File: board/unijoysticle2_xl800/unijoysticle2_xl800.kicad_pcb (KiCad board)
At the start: 4 copper layers, 72 x 53 mm, 54 parts, among them J1 USB_B_Micro, J2 DE9_Receptacle, J3 DE9_Receptacle, Q1 S8050, Q2 S8050, SW1 RESET, SW2 BOOT, SW3 MODE, SW4 SWAP, U1 ESP32-WROOM-32, U2 AMS1117-3.3, U3 CH340C, U4 74HC05, U5 74HC05, U6 74HC05

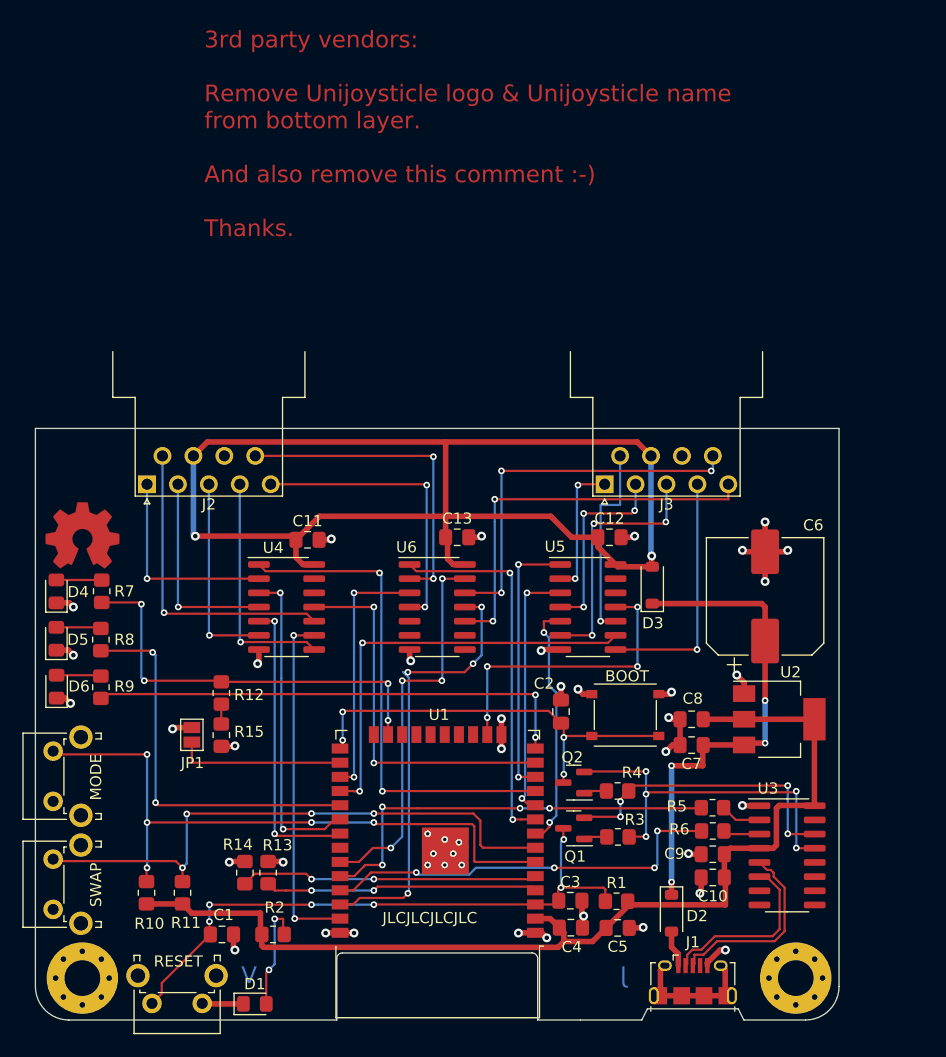
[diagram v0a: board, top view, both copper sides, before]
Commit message: 800XL Rev B.
Support Joy2Bplus buttons: similar to C64 Pot buttons.
GPIO36 Pull-up (instead of Pull-down) so that A500 can be differenciated
from 800XL.
Rounded corners at the top: might be needed if the DE9 connectors is
cut.
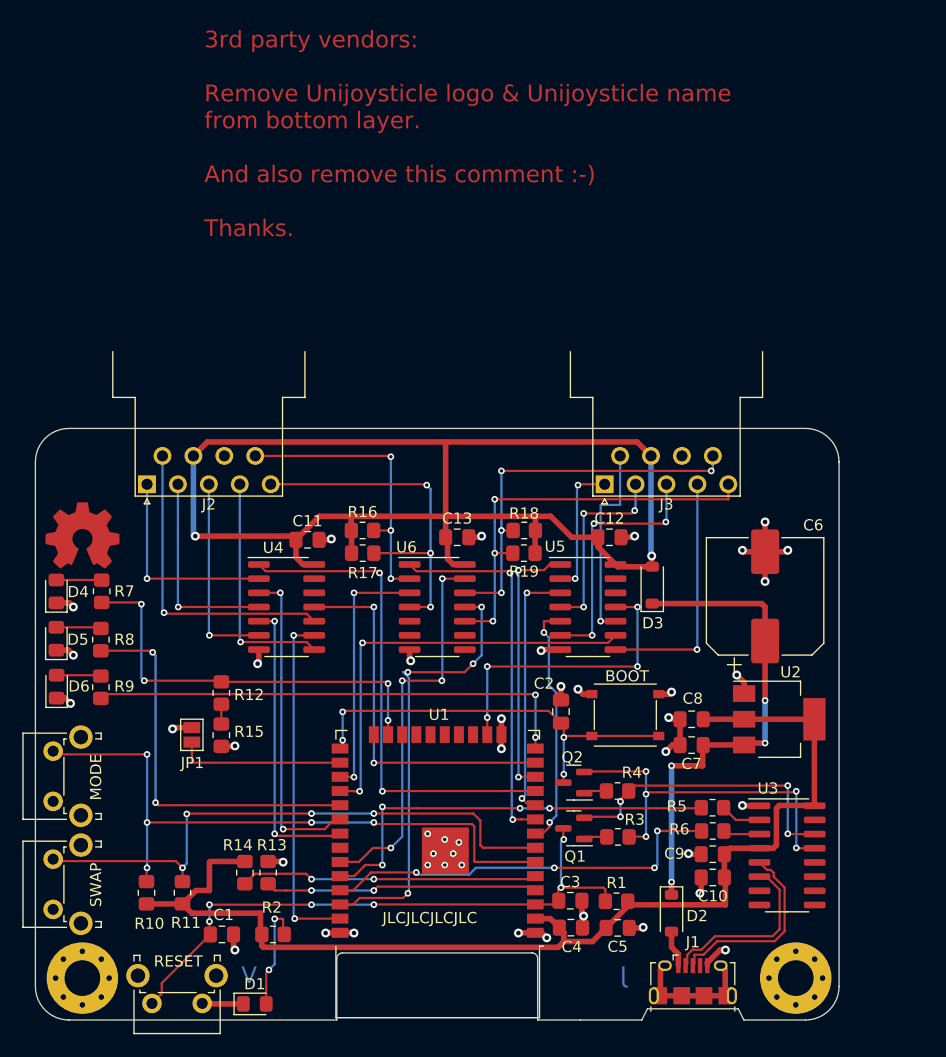
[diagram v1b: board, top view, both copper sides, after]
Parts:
- added R16: 2K7, Resistor_SMD:R_0805_2012Metric_Pad1.20x1.40mm_HandSolder, F.Cu at (106.8, 104.1)
- added R17: 2K7, Resistor_SMD:R_0805_2012Metric_Pad1.20x1.40mm_HandSolder, F.Cu at (106.8, 106.2)
- added R18: 2K7, Resistor_SMD:R_0805_2012Metric_Pad1.20x1.40mm_HandSolder, F.Cu at (121.3, 104.1)
- added R19: 2K7, Resistor_SMD:R_0805_2012Metric_Pad1.20x1.40mm_HandSolder, F.Cu at (121.3, 106.2)
- R14: value 0 -> 10K
- turned R14 to 90 degrees
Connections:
- R14 pad 1: GND -> GPIO_39
- R14 pad 2: GPIO_39 -> +3V3
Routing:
- net +3V3: track 95.2 -> 103.8 mm
- net +5V: track 119.4 -> 126.0 mm
- net /Atari Ports/J1_POTY: track 26.4 -> 32.0 mm, vias 2 -> 3
- net /Atari Ports/J1_POTX: track 29.0 -> 26.3 mm, vias 2 -> 3
- net /Atari Ports/J2_POTY: track 35.8 -> 37.4 mm, vias 2 -> 3
- net GND: track 63.4 -> 62.0 mm, vias 44 -> 43
- net /Atari Ports/J2_POTX: track 34.4 -> 35.5 mm, vias 3 -> 4
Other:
- outline, holes or cut-outs redrawn
- board text added: "Unijoysticle 2 800XL Rev. B"
- board text removed: "Unijoysticle 2 A1000 / 800XL Rev. A"

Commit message: Improved silkscreen for 800XL
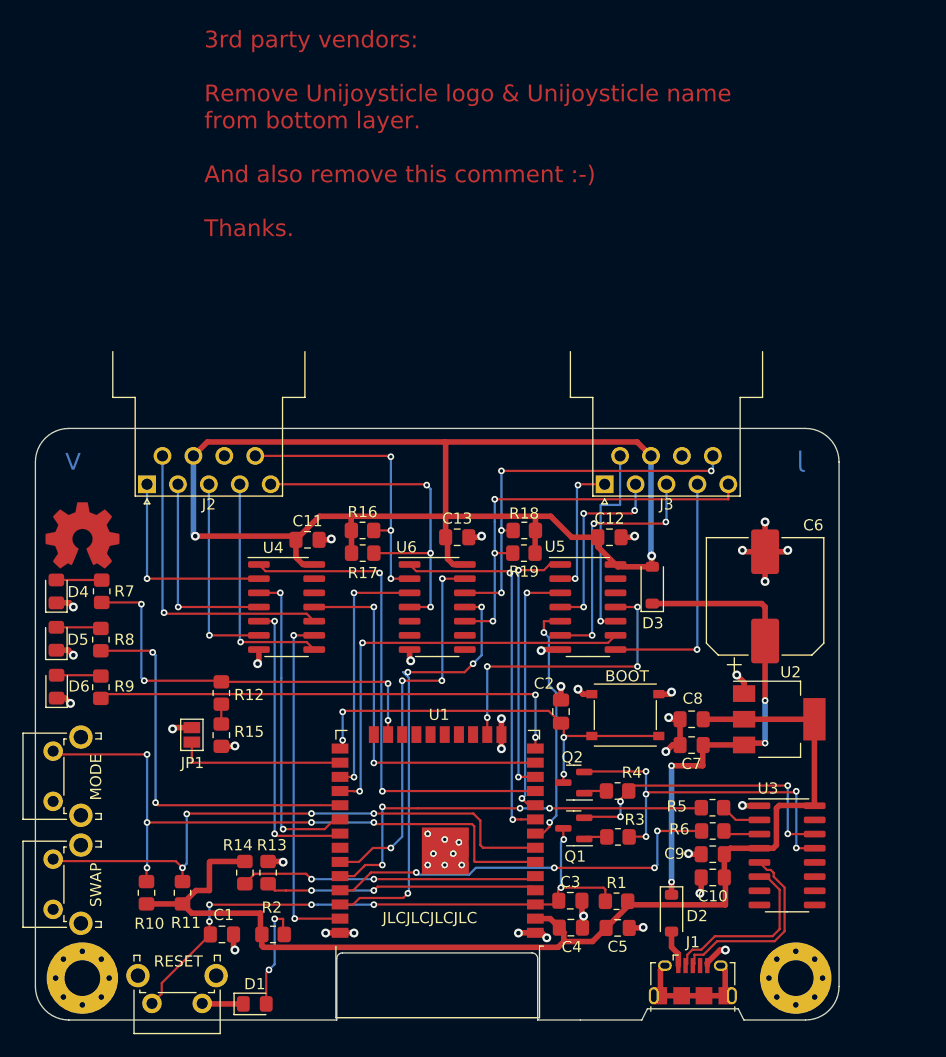
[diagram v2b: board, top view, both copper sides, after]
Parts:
- moved G*** 1.32 mm to (115.3, 112.5)
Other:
- board text added: ". 800XL ."
- board text added: "REV B"
- board text added: "Unijoysticle 2"
- board text added: "©️ 2023 R. Quesada"
- board text removed: "Unijoysticle 2 800XL Rev. B"
- board text removed: "©️ 2023 Ricardo Quesada http://retro.moe"
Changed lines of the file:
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@@
   )
   (footprint "Unijoysticle:unijoysticle_logo" locked (layer "B.Cu")
-    (at 115.443 113.792 180)
+    (at 115.3414 112.4712 180)
     (attr board_only exclude_from_pos_files exclude_from_bom)
     (fp_text reference "G***" (at 0 0) (layer "F.SilkS") hide
@@
     (effects (font (size 1.5 1.5) (thickness 0.3)) (justify left))
   )
-  (gr_text "V" (at 96.647 144) (layer "B.Cu")
+  (gr_text "V" (at 80.8736 98) (layer "B.Cu")
     (effects (font (size 1.5 1.5) (thickness 0.3)))
   )
-  (gr_text "J" (at 130.175 144) (layer "B.Cu")
+  (gr_text "J" (at 146.0246 97.79) (layer "B.Cu")
     (effects (font (size 1.5 1.5) (thickness 0.3)) (justify mirror))
   )
-  (gr_text "Unijoysticle 2\n800XL\nRev. B" (at 113.615 130.73) (layer "B.SilkS")
+  (gr_text "REV                      B" (at 114.681 145.3134) (layer "B.SilkS")
     (effects (font (size 1.5 1.5) (thickness 0.3)) (justify mirror))
   )
-  (gr_text "©️ 2023 Ricardo Quesada\nhttp://retro.moe" (at 113.5634 138.75) (layer "B.SilkS")
+  (gr_text "Unijoysticle 2" (at 123.9774 126.5428) (layer "B.SilkS")
+    (effects (font (size 2 2) (thickness 0.3)) (justify left bottom mirror))
+  )
+  (gr_text "©️ 2023 R. Quesada" (at 78.994 113.5126 270) (layer "B.SilkS")
     (effects (font (size 1.5 1.5) (thickness 0.2)) (justify mirror))
   )
+  (gr_text ".   800XL    .\n\n" (at 203.327 158.496) (layer "B.SilkS" knockout)
+    (effects (font (face "EightBit Atari") (size 10 10) (thickness 0.2) bold) (justify left bottom mirror))
+    (render_cache ".   800XL    .\n\n" 0
+      (polygon
+        (pts
+          (xy 194.377942 139.996)          (xy 198.051354 139.996)          (xy 198.051354 136.322587)          (xy 194.377942 136.322587)
+        )
+      )
+      (polygon
+        (pts
+          (xy 143.809903 131.046942)          (xy 145.568451 131.046942)          (xy 145.568451 132.961806)          (xy 143.809903 132.961806)
+          (xy 143.809903 134.564039)          (xy 145.568451 134.564039)          (xy 145.568451 138.237451)          (xy 143.809903 138.237451)
+          (xy 143.809903 139.996)          (xy 136.619393 139.996)          (xy 136.619393 138.237451)          (xy 134.860845 138.237451)
+          (xy 134.860845 134.720354)          (xy 138.534257 134.720354)          (xy 138.534257 138.081136)          (xy 141.895039 138.081136)
+          (xy 141.895039 134.720354)          (xy 138.534257 134.720354)          (xy 134.860845 134.720354)          (xy 134.860845 134.564039)
+          (xy 136.619393 134.564039)          (xy 136.619393 132.961806)          (xy 134.860845 132.961806)          (xy 134.860845 131.203257)
+          (xy 138.534257 131.203257)          (xy 138.534257 132.80549)          (xy 141.895039 132.80549)          (xy 141.895039 131.203257)
+          (xy 138.534257 131.203257)          (xy 134.860845 131.203257)          (xy 134.860845 131.046942)          (xy 136.619393 131.046942)
+          (xy 136.619393 129.288393)          (xy 143.809903 129.288393)
+        )
+      )
+      (polygon
+        (pts
+          (xy 129.809903 131.046942)          (xy 131.568451 131.046942)          (xy 131.568451 138.237451)          (xy 129.809903 138.237451)
+          (xy 129.809903 139.996)          (xy 122.619393 139.996)          (xy 122.619393 138.237451)          (xy 120.860845 138.237451)
+          (xy 120.860845 138.081136)          (xy 124.534257 138.081136)          (xy 127.895039 138.081136)          (xy 127.895039 136.478903)
+          (xy 126.13649 136.478903)          (xy 126.13649 134.720354)          (xy 124.534257 134.720354)          (xy 124.534257 138.081136)
+          (xy 120.860845 138.081136)          (xy 120.860845 131.203257)          (xy 124.534257 131.203257)          (xy 124.534257 132.80549)
+          (xy 126.292806 132.80549)          (xy 126.292806 134.564039)          (xy 127.895039 134.564039)          (xy 127.895039 131.203257)
+          (xy 124.534257 131.203257)          (xy 120.860845 131.203257)          (xy 120.860845 131.046942)          (xy 122.619393 131.046942)
+          (xy 122.619393 129.288393)          (xy 129.809903 129.288393)
+        )
+      )
+      (polygon
+        (pts
+          (xy 115.809903 131.046942)          (xy 117.568451 131.046942)          (xy 117.568451 138.237451)          (xy 115.809903 138.237451)
+          (xy 115.809903 139.996)          (xy 108.619393 139.996)          (xy 108.619393 138.237451)          (xy 106.860845 138.237451)
+          (xy 106.860845 138.081136)          (xy 110.534257 138.081136)          (xy 113.895039 138.081136)          (xy 113.895039 136.478903)
+          (xy 112.13649 136.478903)          (xy 112.13649 134.720354)          (xy 110.534257 134.720354)          (xy 110.534257 138.081136)
+          (xy 106.860845 138.081136)          (xy 106.860845 131.203257)          (xy 110.534257 131.203257)          (xy 110.534257 132.80549)
+          (xy 112.292806 132.80549)          (xy 112.292806 134.564039)          (xy 113.895039 134.564039)          (xy 113.895039 131.203257)
+          (xy 110.534257 131.203257)          (xy 106.860845 131.203257)          (xy 106.860845 131.046942)          (xy 108.619393 131.046942)
+          (xy 108.619393 129.288393)          (xy 115.809903 129.288393)
+        )
+      )
+      (polygon
+        (pts
+          (xy 92.860845 139.996)          (xy 96.534257 139.996)          (xy 96.534257 136.478903)          (xy 99.895039 136.478903)
+          (xy 99.895039 139.996)          (xy 103.568451 139.996)          (xy 103.568451 136.322587)          (xy 101.809903 136.322587)
+          (xy 101.809903 132.961806)          (xy 103.568451 132.961806)          (xy 103.568451 129.288393)          (xy 99.895039 129.288393)
+          (xy 99.895039 132.80549)          (xy 96.534257 132.80549)          (xy 96.534257 129.288393)          (xy 92.860845 129.288393)
+          (xy 92.860845 132.961806)          (xy 94.619393 132.961806)          (xy 94.619393 136.322587)          (xy 92.860845 136.322587)
+        )
+      )
+      (polygon
+        (pts
+          (xy 78.860845 139.996)          (xy 89.568451 139.996)          (xy 89.568451 129.288393)          (xy 85.895039 129.288393)
+          (xy 85.895039 138.081136)          (xy 78.860845 138.081136)
+        )
+      )
+      (polygon
+        (pts
+          (xy 12.377942 139.996)          (xy 16.051354 139.996)          (xy 16.051354 136.322587)          (xy 12.377942 136.322587)
+        )
+      )
+    )
+  )
   (gr_text "JLCJLCJLCJLC" (at 108.585 139.446) (layer "F.SilkS")

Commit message: Atari 800XL: more fixes in silkscreen
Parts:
- removed the G*** at (115.3, 112.5)
- added G***: LOGO, Unijoysticle:unijoysticle_logo_small, B.Cu at (113.3, 110.6)
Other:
- board text added: "http://retro.moe"
